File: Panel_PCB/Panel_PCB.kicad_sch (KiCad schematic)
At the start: 127 parts, among them J1 AC, J10 Relay 3, J11 Relay 4, J12 AC, J13 AC, J14 + de la bateria, J15 - de la bateria, J2 Bateria, J3 Sensor IN, J4 Sensor OUT, J5 Boton 1, J6 Boton 2, J7 Boton 3, J8 Relay 1, J9 Relay 2, K1 SANYOU_SRD_Form_C, K2 SANYOU_SRD_Form_C, K3 SANYOU_SRD_Form_C, K4 SANYOU_SRD_Form_C, K5 EC2-4.5SNU, K6 SANYOU_SRD_Form_C, K7 SANYOU_SRD_Form_C, Q1 2N2222A, Q2 2N2222A, Q3 2N2222A, Q4 2N2222A, Q5 BC558, Q6 BC558, Q7 2N2222A, U1 TLP291, U10 LM1117T-3.3, U11 LM7812_TO220, U12 DS1307+, U2 TLP291, U3 TLP291, U4 TLP291, U5 LM7812_TO220, U6 LM7812_TO220, U7 LM7805_TO220, U8 LM7805_TO220, U9 LM1117T-3.3

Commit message: Organización de elementos
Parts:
- added D16: 1N4001, Diode_THT:D_DO-41_SOD81_P10.16mm_Horizontal, symbol Diode:1N4001
- added HS1, HS2: Heatsink, Heatsink:Heatsink_125x35x50mm_3xFixationM3, symbol Mechanical:Heatsink
- added Y1: Crystal, Crystal:Crystal_C26-LF_D2.1mm_L6.5mm_Horizontal, symbol Device:Crystal
- D14: footprint (none) -> LED_THT:LED_D3.0mm
- J14, J15: footprint (none) -> TerminalBlock_Phoenix:TerminalBlock_Phoenix_MKDS-1,5-2-5.08_1x02_P5.08mm_Horizontal
- U10, U9: footprint Package_TO_SOT_THT:TO-220-3_Horizontal_TabDown -> Package_TO_SOT_THT:TO-220-3_Vertical
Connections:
- net at GPIO21.1 (Pin_1): now also U12.5 (SDA)
- net at K7.2, R21.1: now also D16.1 (K)
- net at GPIO22.1 (Pin_1): now also U12.6 (SCL)
- net at C10.1, U8.3 (VO), VIN1.1 (Pin_1): now also U12.8 (VCC)
- net at K7.5, Q7.3 (C): now also D16.2 (A)
- net at GND_2.1 (Pin_1): now also BT1.2 (-), U12.4 (GND)
- net at U12.1 (X1): now also Y1.2
- net at U12.2 (X2): now also Y1.1
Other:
- moved on the sheet: BT1, D3, D4, D5, D6, J10, J11, J8, J9, K1, K2, K3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

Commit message: Comparador de voltaje (para el cargador de batería)
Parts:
- removed D12: 11 V, Diode_THT:D_DO-41_SOD81_P10.16mm_Horizontal, symbol Device:D_Zener
- removed D13: 1N4001, Diode_THT:D_DO-41_SOD81_P10.16mm_Horizontal, symbol Diode:1N4001
- removed D14: LED, LED_THT:LED_D3.0mm, symbol Device:LED
- removed J14: + de la bateria, TerminalBlock_Phoenix:TerminalBlock_Phoenix_MKDS-1,5-2-5.08_1x02_P5.08mm_Horizontal, symbol Connector:Screw_Terminal_01x01
- removed J15: - de la bateria, TerminalBlock_Phoenix:TerminalBlock_Phoenix_MKDS-1,5-2-5.08_1x02_P5.08mm_Horizontal, symbol Connector:Screw_Terminal_01x01
- removed Q5, Q6: BC558, Package_TO_SOT_THT:TO-92_Inline, symbol Transistor_BJT:BC558
- removed R20: 10K, Resistor_THT:R_Axial_DIN0309_L9.0mm_D3.2mm_P12.70mm_Horizontal, symbol Device:R_US
- removed R22: 330K, Resistor_THT:R_Axial_DIN0309_L9.0mm_D3.2mm_P12.70mm_Horizontal, symbol Device:R_US
- added U13: LM311, Package_DIP:DIP-8_W7.62mm, symbol Comparator:LM311
- R17: value 330K -> 1K
- R18: value 4.3K -> 2K
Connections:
- net at C1.2, C10.2, C11.2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: now also C15.2, C16.2, D10.1 (K), R21.2, U13.1 (GND)
- net at C12.1, GPIO34.1 (Pin_1), GPIO35.1 (Pin_1)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: now also R18.1
- net at R19.2: now also GPIO18.1 (Pin_1)
- net at R17.1: now also D16.1 (K), K7.5
- net at D7.2 (A), J2.1 (Pin_1): now also R16.2, U13.3 (-)
- net at C4.1, C7.1, C9.1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: now also U13.2 (+)
- net at Q7.1 (E): now also R21.1; no longer R18.1
- net at R17.2: now also C1.1, K5.4, R1.2; no longer R18.2
- net at D16.2 (A), Q7.3 (C): now also K7.2; no longer K7.5
- net at GPIO39.1 (Pin_1): now also R18.2, U13.7
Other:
- note added: "Habilita el uso de la bateria a los reles de las salidas"
- note removed: "+ de la bateria"
- note removed: "- de la bateria"
- note removed: "Habilita el uso de la bateria a los reles"
- moved on the sheet: C15, C16, D10, D11, D15, D16, HS1, HS2, K5, K7, Q7, R15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

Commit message: Nuevo esquematico (falta boost converter de 12V a 13.5V
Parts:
- removed C1: 35V 4700μF, Capacitor_THT:C_Radial_D18.0mm_H35.5mm_P7.50mm, symbol Device:C_US
- removed C3, C5: 0.22 μF, Capacitor_THT:C_Disc_D3.0mm_W1.6mm_P2.50mm, symbol Device:C_US
- removed C4, C6: 0.1 μF, Capacitor_THT:C_Disc_D3.0mm_W1.6mm_P2.50mm, symbol Device:C_US
- removed D1: KBP204G, Diode_THT:Diode_Bridge_Vishay_KBPM, symbol Device:D_Bridge_+AA-
- removed F2: Fuse_Small, Fuse:Fuseholder_Cylinder-5x20mm_Schurter_0031_8201_Horizontal_Open, symbol Device:Fuse_Small
- removed HS2: Heatsink, Heatsink:Heatsink_125x35x50mm_3xFixationM3, symbol Mechanical:Heatsink
- removed J12, J13: AC, TerminalBlock_Phoenix:TerminalBlock_Phoenix_MKDS-1,5-2-5.08_1x02_P5.08mm_Horizontal, symbol Connector:Screw_Terminal_01x02
- removed K6: SANYOU_SRD_Form_C, Relay_THT:Relay_SPDT_SANYOU_SRD_Series_Form_C, symbol Relay:SANYOU_SRD_Form_C
- removed R1: 100 Ω 2W, Resistor_THT:R_Axial_DIN0617_L17.0mm_D6.0mm_P25.40mm_Horizontal, symbol Device:R_US
- removed U5, U6: LM7812_TO220, Package_TO_SOT_THT:TO-220-3_Vertical, symbol Regulator_Linear:LM7812_TO220
- added D1: 1N4001, Diode_THT:D_DO-41_SOD81_P10.16mm_Horizontal, symbol Diode:1N4001
- J1: value AC -> DC
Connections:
- net at C10.2, C11.2, C12.2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: now also D8.2 (A), K5.12, U13.4 (V-)
- net at K5.4, R17.2: now also D9.2 (A), K5.1, D1.1 (K)
- net at C2.1, D2.1 (K), R2.2: now also C7.1, C9.1, D3.1 (K), D4.1 (K), D5.1 (K), D6.1 (K), K1.5, K2.5, K3.5, K4.5, R10.1, R4.1, R6.1, R8.1, U13.8 (V+), U7.1 (VI), U8.1 (VI)
- net at K5.5, R2.1: now also K5.9; no longer K7.1
- net at F1.2: now also D1.2 (A); no longer K5.1
- net at J1.1 (Pin_1): now also D8.1 (K); no longer K5.12
- new net: D9.1 (K), U13.2 (+)
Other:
- note added: "entrada DC o bateria"
- note removed: "120 VAC"
- note removed: "AC o bateria"
- note removed: "Con bateria no se usan los LM7812"
- note removed: "Habilita el uso de la bateria a los reles de las salidas"
- note removed: "Transformador"
- moved on the sheet: J1, J3, J4

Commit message: Ajustes al esquemático
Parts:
- added R1, R20, R22, R23: 330, Resistor_THT:R_Axial_DIN0207_L6.3mm_D2.5mm_P10.16mm_Horizontal, symbol Device:R_US
- R19: value 6.8K -> 330
- R3, R5, R7, R9: value 100 -> 1000
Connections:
- net at U2.1: now also R20.2; no longer GPIO32.1 (Pin_1)
- net at U3.1: now also R22.2; no longer GPIO33.1 (Pin_1)
- net at U4.1: now also R23.2; no longer GPIO25.1 (Pin_1)
- net at U1.1: now also R1.2; no longer GPIO23.1 (Pin_1)
- new net: GPIO32.1 (Pin_1), R20.1
- new net: GPIO33.1 (Pin_1), R22.1
- new net: GPIO25.1 (Pin_1), R23.1
- new net: GPIO23.1 (Pin_1), R1.1

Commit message: Actualización de placa
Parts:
- removed 3V3, EN1, GND_1, GND_2, GPIO1, GPIO12, GPIO13, GPIO14, GPIO15, GPIO16, GPIO17, GPIO18, GPIO19, GPIO2, GPIO21, GPIO22, GPIO23, GPIO25, GPIO26, GPIO27, GPIO3, GPIO32, GPIO33, GPIO34, GPIO35, GPIO36, GPIO39, GPIO4, GPIO5, VIN1: ~, Connector_Wire:SolderWire-0.75sqmm_1x01_D1.25mm_OD2.3mm, symbol Connector:Screw_Terminal_01x01
- added J12: Terminal A, TerminalBlock:TerminalBlock_Xinya_XY308-2.54-15P_1x15_P2.54mm_Horizontal, symbol Connector:Screw_Terminal_01x15
- added J13: Terminal B, TerminalBlock:TerminalBlock_Xinya_XY308-2.54-15P_1x15_P2.54mm_Horizontal, symbol Connector:Screw_Terminal_01x15
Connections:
- net at C10.2, C11.2, C12.2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: now also J12.2 (Pin_2)
- net at C12.1, J3.2 (Pin_2), J4.2 (Pin_2)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: now also J13.4 (Pin_4), J13.5 (Pin_5)
- net at R18.2, U13.7: now also J13.3 (Pin_3)
- net at U12.5 (SDA): now also J12.11 (Pin_11)
- net at C14.1, J5.2 (Pin_2), J6.2 (Pin_2)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: now also J13.10 (Pin_10), J13.11 (Pin_11), J13.9 (Pin_9)
- net at R20.1: now also J13.6 (Pin_6)
- net at U12.6 (SCL): now also J12.14 (Pin_14)
- net at C10.1, U12.8 (VCC), U8.3 (VO): now also J13.15 (Pin_15)
- net at R22.1: now also J13.7 (Pin_7)
- net at R19.2: now also J12.9 (Pin_9)
- net at BT1.2 (-), U12.4 (GND): now also J13.14 (Pin_14)
- net at R23.1: now also J13.8 (Pin_8)
- net at R1.1: now also J12.15 (Pin_15)
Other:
- note added: "3V3 GND_1 GPIO15 GPIO2 GPIO4 GPIO16 GPIO17 GPIO5 GPIO18 GPIO19 GPIO21 GPIO3 GPIO1 GPIO22 GPIO23"
- note added: "VIN1 GND_2 GPIO13 GPIO12 GPIO14 GPIO27 GPIO26 GPIO25 GPIO33 GPIO32 GPIO35 GPIO34 GPIO39 GPIO36 EN1"

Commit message: Actualización de esquematico
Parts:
- added D12, D13: 1N4001, Diode_THT:D_DO-41_SOD81_P10.16mm_Horizontal, symbol Diode:1N4001
- added R24, R25: 10K, Resistor_THT:R_Axial_DIN0207_L6.3mm_D2.5mm_P10.16mm_Horizontal, symbol Device:R_US
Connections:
- net at D1.1 (K), K5.1, K5.4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: no longer D9.2 (A)
- net at D7.2 (A), J2.1 (Pin_1), R16.2: no longer U13.3 (-)
- net at C2.1, C7.1, C9.1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: now also D9.2 (A)
- net at C10.1, J13.15 (Pin_15), U12.8 (VCC)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: now also J12.11 (Pin_11), J12.14 (Pin_14), R24.1, R25.2
- net at D9.1 (K): now also D12.2 (A); no longer U13.2 (+)
- net at U12.5 (SDA): now also R25.1; no longer J12.11 (Pin_11)
- net at U12.6 (SCL): now also R24.2; no longer J12.14 (Pin_14)
- net at U12.1 (X1): now also Y1.1; no longer Y1.2
- net at U12.2 (X2): now also Y1.2; no longer Y1.1
- new net: D12.1 (K), D13.2 (A)
- new net: D13.1 (K), U13.2 (+)
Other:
- note added: "Debido a los diodos anteriores se debe virificar si hay 12V exactos"
- note added: "si empieza a cargar a este pin le llegan más de 13V entonces se superaria el voltaje de alimentación esto no es recomendable, SOLUCIONARLO!!!"
- moved on the sheet: BT1, D9, U12, Y1

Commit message: Actualización de esquematico
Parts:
- added C1: 100 μF, Capacitor_THT:C_Disc_D3.0mm_W1.6mm_P2.50mm, symbol Device:C_US
- added C3: 10 μF, Capacitor_THT:C_Disc_D3.0mm_W1.6mm_P2.50mm, symbol Device:C_US
- added D14, D17, D18: 1N4001, Diode_THT:D_DO-41_SOD81_P10.16mm_Horizontal, symbol Diode:1N4001
- added R26: 10K, Resistor_THT:R_Axial_DIN0309_L9.0mm_D3.2mm_P12.70mm_Horizontal, symbol Device:R_US
- added U5: LM7805_TO220, Package_TO_SOT_THT:TO-220-3_Vertical, symbol Regulator_Linear:LM7805_TO220
- added U6: LM1117T-3.3, Package_TO_SOT_THT:TO-220-3_Vertical, symbol Regulator_Linear:LM1117T-3.3
- R18: value 2K -> 10K
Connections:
- net at C10.2, C11.2, C12.2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: now also C1.2, C3.2, D17.1 (K), R26.2, U5.2 (GND), U6.1 (GND); no longer D10.1 (K), U13.1 (GND)
- net at D12.1 (K): now also R18.1, U13.8 (V+), D14.2 (A); no longer D13.2 (A)
- net at C12.1, J13.4 (Pin_4), J13.5 (Pin_5)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: no longer R18.1
- net at R18.2, U13.7: no longer J13.3 (Pin_3)
- net at D7.1 (K), K5.10: now also D18.2 (A)
- net at C2.1, C7.1, C9.1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: no longer U13.8 (V+)
- net at U13.2 (+): now also D18.1 (K); no longer D13.1 (K)
- net at U13.3 (-): now also D13.1 (K)
- new net: D10.1 (K), D17.2 (A)
- new net: C1.1, U5.3 (VO), U6.3 (VI)
- new net: R26.1, U13.1 (GND), U5.1 (VI)
- new net: D13.2 (A), D14.1 (K)
- new net: C3.1, J13.3 (Pin_3), U6.2 (VO)
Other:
- note added: "Luz emergencia"
- note added: "Puerta 1"
- note added: "Puerta 2"
- note added: "Se necesitan al menos 14 VDC"
- note added: "Señal panico"
- note removed: "Relay 1"
- note removed: "Relay 2"
- note removed: "Relay 3"
- note removed: "Relay 4"
- note removed: "si empieza a cargar a este pin le llegan más de 13V entonces se superaria el voltaje de alimentación esto no es recomendable, SOLUCIONARLO!!!"
- moved on the sheet: D10, D11, D12, D13, D9, R16, R18

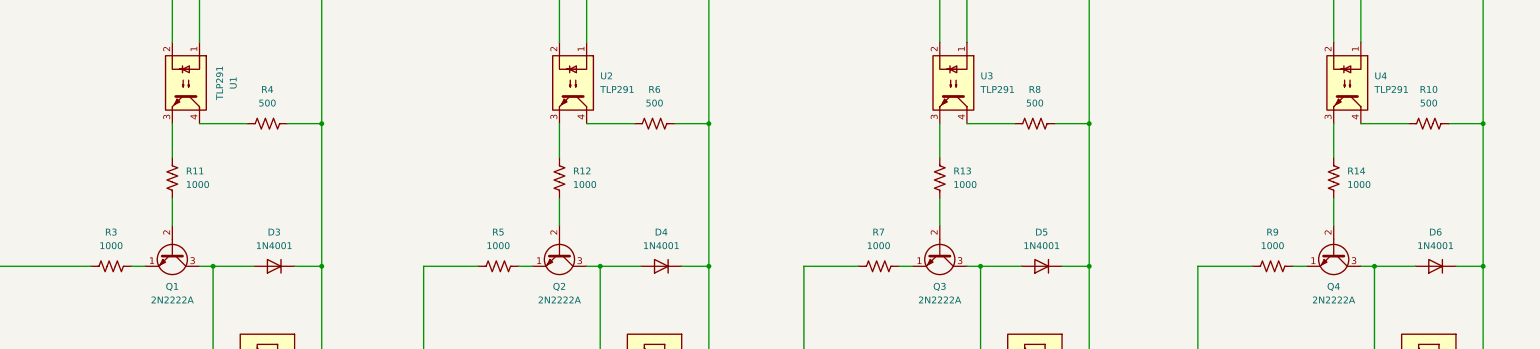
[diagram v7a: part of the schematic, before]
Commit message: Entradas (sensores y botones). Salidas (relés)
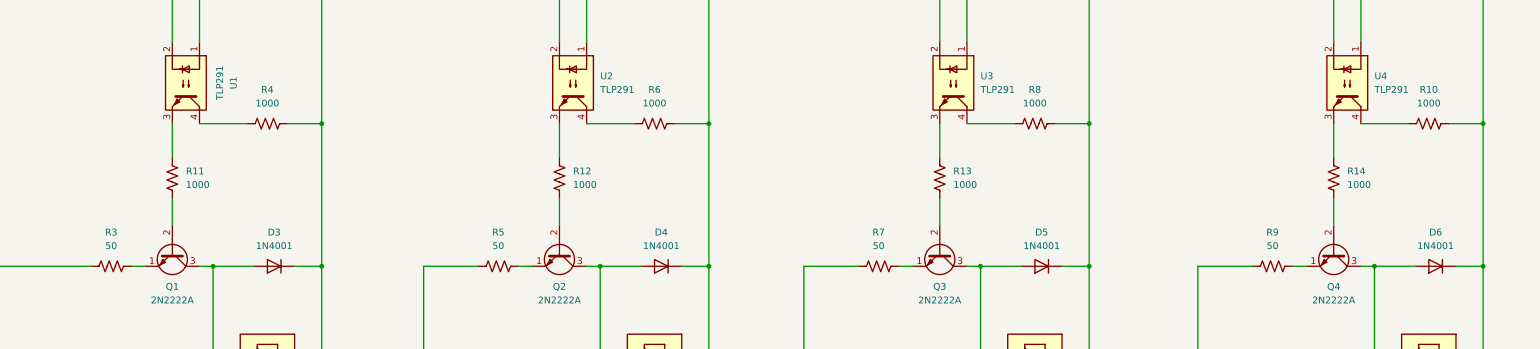
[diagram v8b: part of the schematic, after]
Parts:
- R10, R4, R6, R8: value 500 -> 1000
- R3, R5, R7, R9: value 1000 -> 50; footprint Resistor_THT:R_Axial_DIN0207_L6.3mm_D2.5mm_P10.16mm_Horizontal -> Resistor_THT:R_Axial_DIN0309_L9.0mm_D3.2mm_P12.70mm_Horizontal
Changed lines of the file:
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@@
 			)
 		)
-		(property "Value" "500"
+		(property "Value" "1000"
 			(at 560.07 378.46 90)
 			(effects
@@
 			)
 		)
-		(property "Value" "1000"
+		(property "Value" "50"
 			(at 387.35 405.13 90)
 			(effects
@@
 			)
 		)
-		(property "Footprint" "Resistor_THT:R_Axial_DIN0207_L6.3mm_D2.5mm_P10.16mm_Horizontal"
+		(property "Footprint" "Resistor_THT:R_Axial_DIN0309_L9.0mm_D3.2mm_P12.70mm_Horizontal"
 			(at 387.096 409.956 90)
 			(effects
@@
 			)
 		)
-		(property "Value" "500"
+		(property "Value" "1000"
 			(at 633.73 378.46 90)
 			(effects
@@
 			)
 		)
-		(property "Value" "1000"
+		(property "Value" "50"
 			(at 459.74 405.13 90)
 			(effects
@@
 			)
 		)
-		(property "Footprint" "Resistor_THT:R_Axial_DIN0207_L6.3mm_D2.5mm_P10.16mm_Horizontal"
+		(property "Footprint" "Resistor_THT:R_Axial_DIN0309_L9.0mm_D3.2mm_P12.70mm_Horizontal"
 			(at 459.486 409.956 90)
 			(effects
@@
 			)
 		)
-		(property "Value" "500"
+		(property "Value" "1000"
 			(at 416.56 378.46 90)
 			(effects
@@
 			)
 		)
-		(property "Value" "500"
+		(property "Value" "1000"
 			(at 488.95 378.46 90)
 			(effects
@@
 			)
 		)
-		(property "Value" "1000"
+		(property "Value" "50"
 			(at 604.52 405.13 90)
 			(effects
@@
 			)
 		)
-		(property "Footprint" "Resistor_THT:R_Axial_DIN0207_L6.3mm_D2.5mm_P10.16mm_Horizontal"
+		(property "Footprint" "Resistor_THT:R_Axial_DIN0309_L9.0mm_D3.2mm_P12.70mm_Horizontal"
 			(at 604.266 409.956 90)
 			(effects
@@
 			)
 		)
-		(property "Value" "1000"
+		(property "Value" "50"
 			(at 530.86 405.13 90)
 			(effects
@@
 			)
 		)
-		(property "Footprint" "Resistor_THT:R_Axial_DIN0207_L6.3mm_D2.5mm_P10.16mm_Horizontal"
+		(property "Footprint" "Resistor_THT:R_Axial_DIN0309_L9.0mm_D3.2mm_P12.70mm_Horizontal"
 			(at 530.606 409.956 90)
 			(effects
